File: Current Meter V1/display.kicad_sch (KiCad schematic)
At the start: 4 parts, among them J2 I2C OLED Display Connector, U1 STM32L552ZET6Q

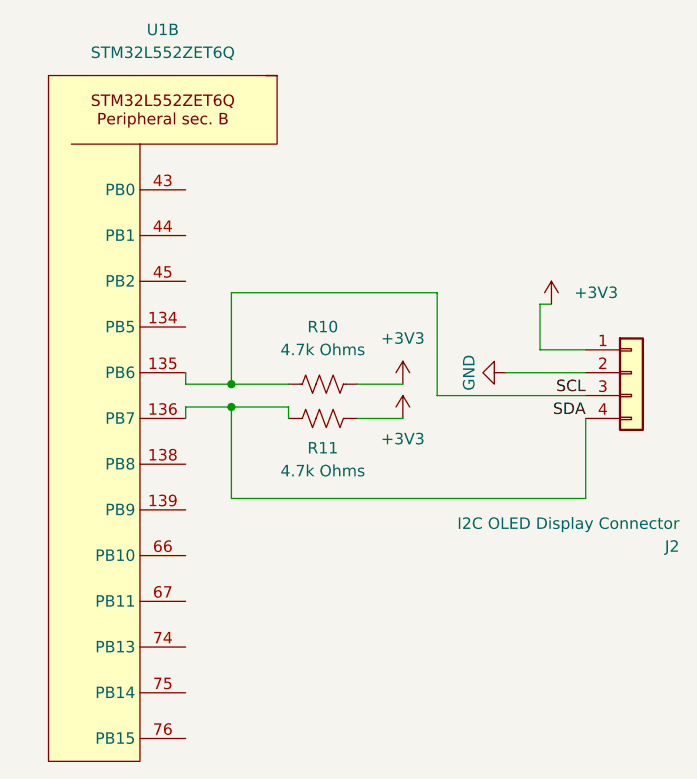
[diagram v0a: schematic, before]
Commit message: Redesign op amp circuit for 0-3.3v output previous design clipped to negative
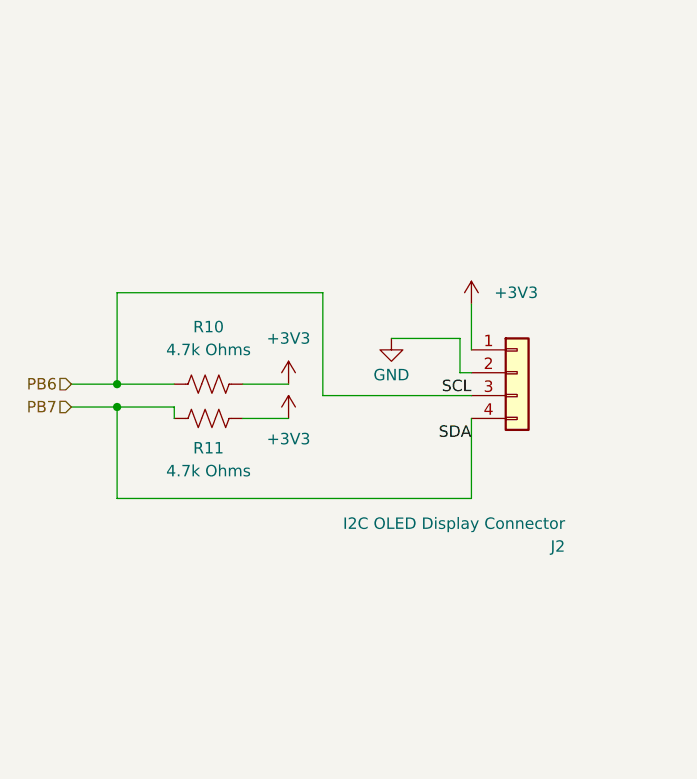
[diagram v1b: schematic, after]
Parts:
- removed U1: STM32L552ZET6Q, Package_QFP:LQFP-144_20x20mm_P0.5mm, symbol bfr_microcontrollers:STM32L552ZET6Q
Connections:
- net SCL renamed PB6
- net SDA renamed PB7
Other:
- moved on the sheet: J2, R10, R11
